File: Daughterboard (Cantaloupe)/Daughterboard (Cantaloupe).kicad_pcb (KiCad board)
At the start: 2 copper layers, 145 x 120.7 mm, 55 parts, among them J3 Pogo, SW1 MX/Choc, SW10 MX/Choc, SW11 MX/Choc, SW12 MX/Choc, SW13 MX/Choc, SW14 MX/Choc, SW15 MX/Choc, SW16 MX/Choc, SW17 MX/Choc, SW18 MX/Choc, SW19 MX/Choc, SW2 MX/Choc, SW20 MX/Choc, SW21 MX/Choc, SW22 MX/Choc, SW23 MX/Choc, SW24 MX/Choc, SW25 MX/Choc, SW26 MX/Choc, SW27 MX/Choc, SW28 MX/Choc, SW29 MX/Choc, SW3 MX/Choc, SW30 MX/Choc, SW31 MX/Choc, SW4 MX/Choc, SW5 MX/Choc, SW6 MX/Choc, SW7 MX/Choc, SW8 MX/Choc, SW9 MX/Choc, U1 74HC595, U2 74HC595, U3 74HC595, U4 74HC595

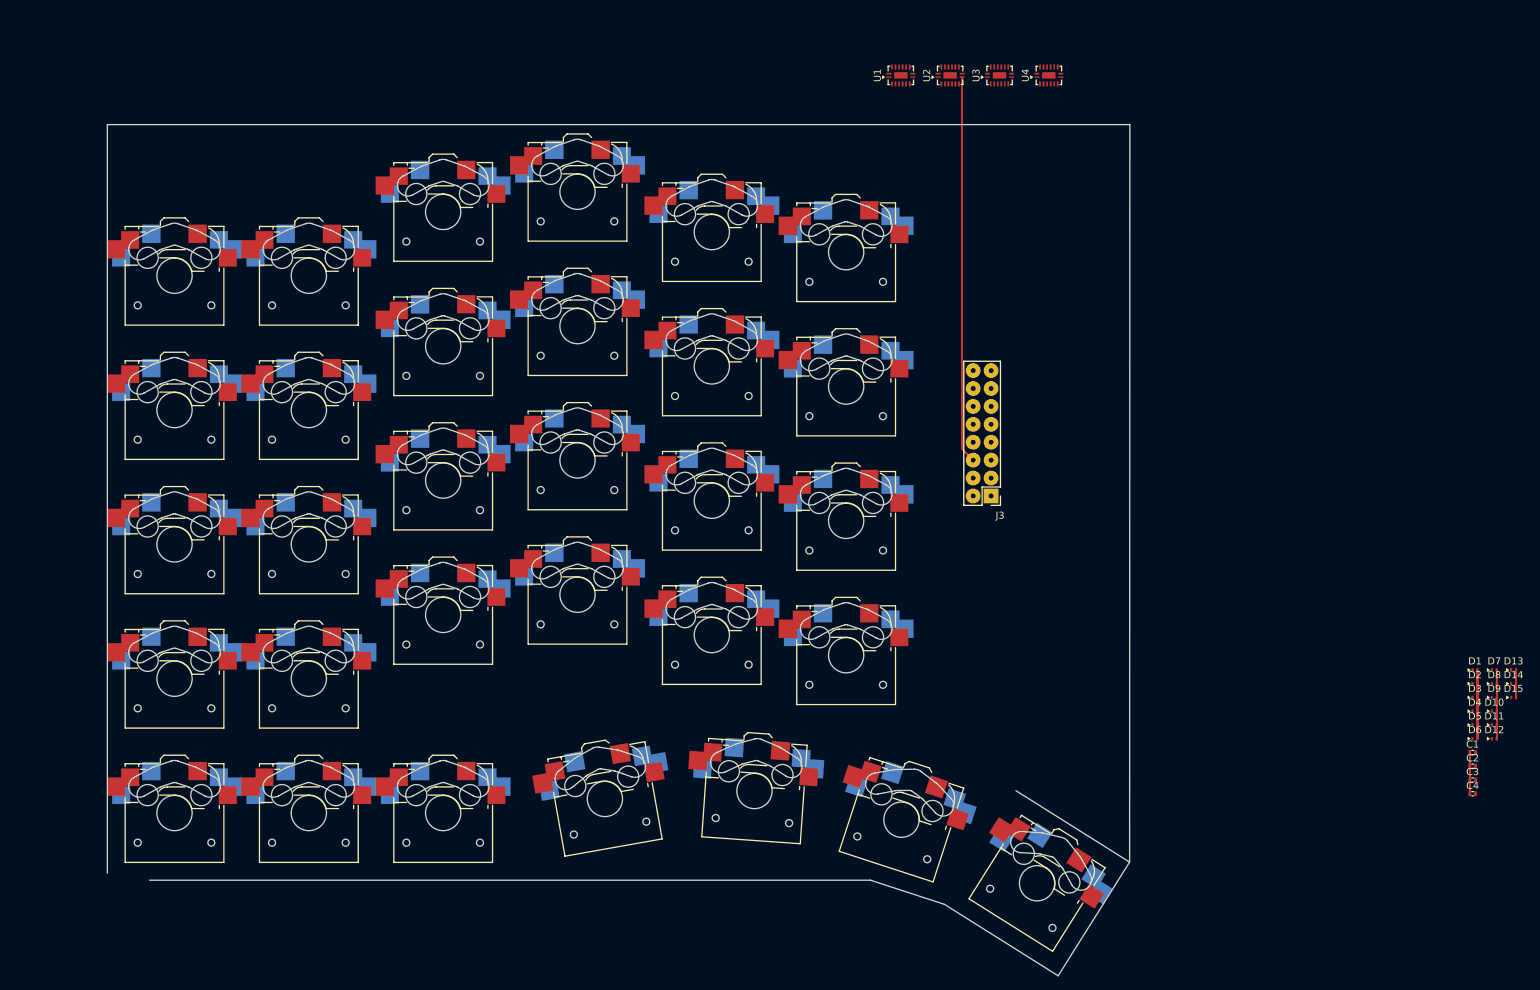
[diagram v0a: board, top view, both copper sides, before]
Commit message: 2026/09/30: V0.4 motherboard update complete
Removed guard ring around the edge of the board. Moved reset button and pogo header down the board. Increased length back to 50mm to allow for an E73-2G4M08S1C version to be developed if desired. Simplified reset circuit - doesn't use the Acheron version anymore. Reduced number of pins in pogo header, as the largest available ones are 2x06. Pinout of pogo header changed to greatly simplify routing - no longer VIK-compliant. Signalis reference and Paw-Connect added back. Changed file structure.
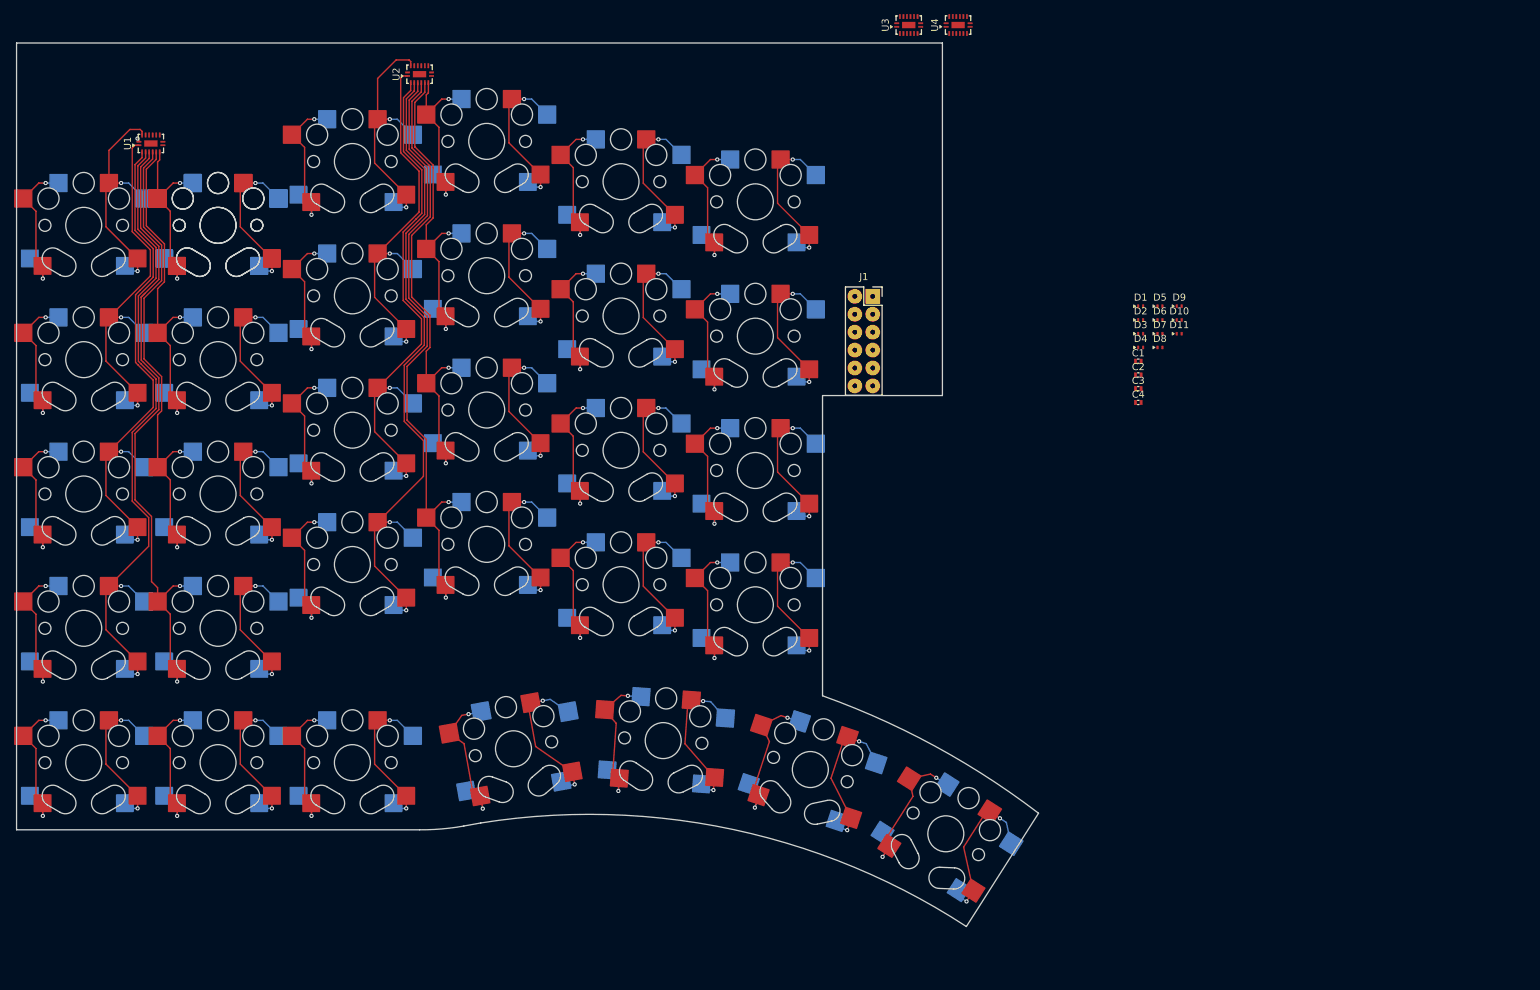
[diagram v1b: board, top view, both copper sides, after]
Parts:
- removed D12, D13: ESD441, GB-Package:X1SON_0.6x1mm_P0.65mm_Texas_DPY0002A
- removed D14, D15: ESD321, GB-Package:X1SON_0.6x1mm_P0.65mm_Texas_DPY0002A
- removed J3: Pogo, GB-Header:PinHeader_2x08_2.54mm_MillMax_PogoPin_823-22-016-10-002101_Double_Sided
- removed the SW1 at (95.2, 38.1)
- added J1: Pogo, GB-Header:PinHeader_2x06_2.54mm_MillMax_PogoPin_823-22-012-10-000101-Double_Sided, F.Cu at (137.1, 52.9)
- added REF**: Breakout_GhostlyButterfly_Galia-G0B1, GB-Breakout:Breakout_GhostlyButterfly_Galia-G0B1, F.Cu at (130.0, 30.0)
- added SW1: MX/Choc, GB-Switch:SW_KB_Choc-KS33_1U_Hotswap_Reversible, B.Cu at (44.3, 42.9)
- added SW1: MX/Choc, GB-Switch:SW_KB_Choc-KS33_1U_Hotswap_Reversible, B.Cu at (25.2, 42.9)
- D1, D10, D2, D4, D5, D6, D7, D8, D9: value ESD441 -> ESD321
- SW10, SW11, SW12, SW13, SW14, SW15, SW16, SW17, SW18, SW19, SW2, SW20, SW21, SW22, SW23, SW24, SW25, SW26, SW27, SW28, SW29, SW3, SW30, SW31, SW4, SW5, SW6, SW7, SW8, SW9: footprint GB-Switch:SW_MX-Choc_1U_Hotswap_Flippable -> GB-Switch:SW_KB_Choc-KS33_1U_Hotswap_Reversible; moved to B.Cu
- moved SW4 120.6 mm to (25.2, 100.0), turned to 180 degrees
- moved SW26 107.3 mm to (120.5, 39.5), turned to 180 degrees
- moved U1 106.8 mm to (34.8, 31.2)
- moved SW10 103.8 mm to (44.3, 119.1), turned to 180 degrees
- moved SW3 96.5 mm to (25.2, 81.0), turned to 180 degrees
- moved SW27 80.8 mm to (120.5, 58.6), turned to 180 degrees
- moved SW9 79.3 mm to (44.3, 100.0), turned to 180 degrees
- moved U2 75.3 mm to (72.8, 21.4)
- moved D6 74.3 mm to (177.8, 56.3)
- moved D5 74.3 mm to (177.8, 54.3)
- moved SW16 74.1 mm to (82.4, 31.0), turned to 180 degrees
- moved C1 73.0 mm to (174.8, 62.1)
- moved C2 73.0 mm to (174.8, 64.1)
- moved C3 73.0 mm to (174.8, 66.0)
- moved C4 73.0 mm to (174.8, 68.0)
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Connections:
- D1 pad 1: RST -> GPIO1
- D10 pad 1: GPIO4 -> SPI_MISO
- D2 pad 1: GPIO3 -> GPIO2
- D3 pad 1: +3V3 -> GPIO3
- D4 pad 1: I2C_SDA -> GPIO4
- D5 pad 1: RGB_DAT -> GPIO5
- D6 pad 1: GPIO1 -> VDD
- D7 pad 1: GPIO -> SPI_CS
- D8 pad 1: SPI_MISO -> SPI_SCK
- D9 pad 1: GPIO5 -> SPI_MOSI
- SW16 pad 1: K14 -> GPIO5
- SW16 pad 2: GPIO5 -> K14
- SW17 pad 1: K15 -> GPIO5
- SW17 pad 2: GPIO5 -> K15
- SW18 pad 1: K17 -> GPIO5
- SW18 pad 2: GPIO5 -> K16
- SW19 pad 1: K16 -> GPIO5
- SW19 pad 2: GPIO5 -> K17
- SW26 pad 1: K24 -> GPIO5
- SW26 pad 2: GPIO5 -> K24
- SW27 pad 1: K25 -> GPIO5
- SW27 pad 2: GPIO5 -> K25
- SW28 pad 1: K26 -> GPIO5
- SW28 pad 2: GPIO5 -> K26
- SW29 pad 1: K27 -> GPIO5
- SW29 pad 2: GPIO5 -> K27
- SW6 pad 1: K04 -> GPIO5
- SW6 pad 2: GPIO5 -> K04
- SW7 pad 1: K05 -> GPIO5
- SW7 pad 2: GPIO5 -> K05
- SW8 pad 1: K06 -> GPIO5
- SW8 pad 2: GPIO5 -> K06
- SW9 pad 1: K07 -> GPIO5
- SW9 pad 2: GPIO5 -> K07
- U1 pad 4: K04 -> K07
- U1 pad 5: K05 -> K06
- U1 pad 6: K06 -> K05
- U1 pad 7: K07 -> K04
- U2 pad 4: K14 -> K17
- U2 pad 5: K15 -> K16
- U2 pad 6: K16 -> K15
- U2 pad 7: K17 -> K14
- U3 pad 4: K24 -> K27
- U3 pad 5: K25 -> K26
- U3 pad 6: K26 -> K25
- U3 pad 7: K27 -> K24
- U4 pad 4: K34 -> K37
- U4 pad 5: K35 -> K36
- U4 pad 6: K36 -> K35
- U4 pad 7: K37 -> K34
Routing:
- net GPIO5: track 0.00 -> 648.1 mm, vias 0 -> 62
- net GND: track 505.2 -> 0.00 mm
- net K13: track 0.00 -> 93.1 mm, vias 0 -> 2
- net K03: track 0.00 -> 91.9 mm, vias 0 -> 2
- net K07: track 0.00 -> 91.1 mm, vias 0 -> 2
- net K17: track 0.00 -> 88.0 mm, vias 0 -> 2
- net K12: track 0.00 -> 71.6 mm, vias 0 -> 2
- net K02: track 0.00 -> 70.8 mm, vias 0 -> 2
- net K06: track 0.00 -> 69.8 mm, vias 0 -> 2
- net K16: track 0.00 -> 66.9 mm, vias 0 -> 2
- net K00: track 0.00 -> 55.4 mm, vias 0 -> 4
- net K11: track 0.00 -> 51.6 mm, vias 0 -> 2
- net K01: track 0.00 -> 50.7 mm, vias 0 -> 2
- net K05: track 0.00 -> 48.5 mm, vias 0 -> 2
- net K15: track 0.00 -> 45.9 mm, vias 0 -> 2
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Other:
- board size 145 x 120.7 mm -> 144.9 x 125.3 mm
- board text removed: "SWITCH"

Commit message: 2026/10/01: Changed library name and updated paths
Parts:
- C1, C2, C3, C4: footprint GB-Device:C_0402_1005Metric -> Kaleidogeist-Device:C_0402_1005Metric
- D1, D10, D11, D2, D3, D4, D5, D6, D7, D8, D9: footprint GB-Package:X1SON_0.6x1mm_P0.65mm_Texas_DPY0002A -> Kaleidogeist-Package:X1SON_0.6x1mm_P0.65mm_Texas_DPY0002A
- J1: footprint GB-Header:PinHeader_2x06_2.54mm_MillMax_PogoPin_823-22-012-10-000101-Double_Sided -> Kaleidogeist-Header:PinHeader_2x06_2.54mm_MillMax_PogoPin_823-22-012-10-000101-Double_Sided
- REF**: footprint GB-Breakout:Breakout_GhostlyButterfly_Galia-G0B1 -> Kaleidogeist-Breakout:Breakout_GhostlyButterfly_Galia-G0B1
- SW1 (x2), SW10, SW11, SW12, SW13, SW14, SW15, SW16, SW17, SW18, SW19, SW2, SW20, SW21, SW22, SW23, SW24, SW25, SW26, SW27, SW28, SW29, SW3, SW30, SW31, SW4, SW5, SW6, SW7, SW8, SW9: footprint GB-Switch:SW_KB_Choc-KS33_1U_Hotswap_Reversible -> Kaleidogeist-Switch:SW_KB_Choc-KS33_1U_Hotswap_Reversible
- U1, U2, U3, U4: footprint GB-Package:DHVQFN-16-1EP_2.5x3.5mm_P0.5mm_EP1x2mm -> Kaleidogeist-Package:DHVQFN-16-1EP_2.5x3.5mm_P0.5mm_EP1x2mm
